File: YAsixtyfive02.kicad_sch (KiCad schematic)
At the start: 64 parts, among them J1 ~{NMI}, J2 Aux 5VDC, J3 Power 5V, J4 Expansion Bus, J7 GND, J8 FTDI Serial2USB, SW1 RESET, SW2 SW_Push_DPDT, U1 WD65C02, U10 74LS138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

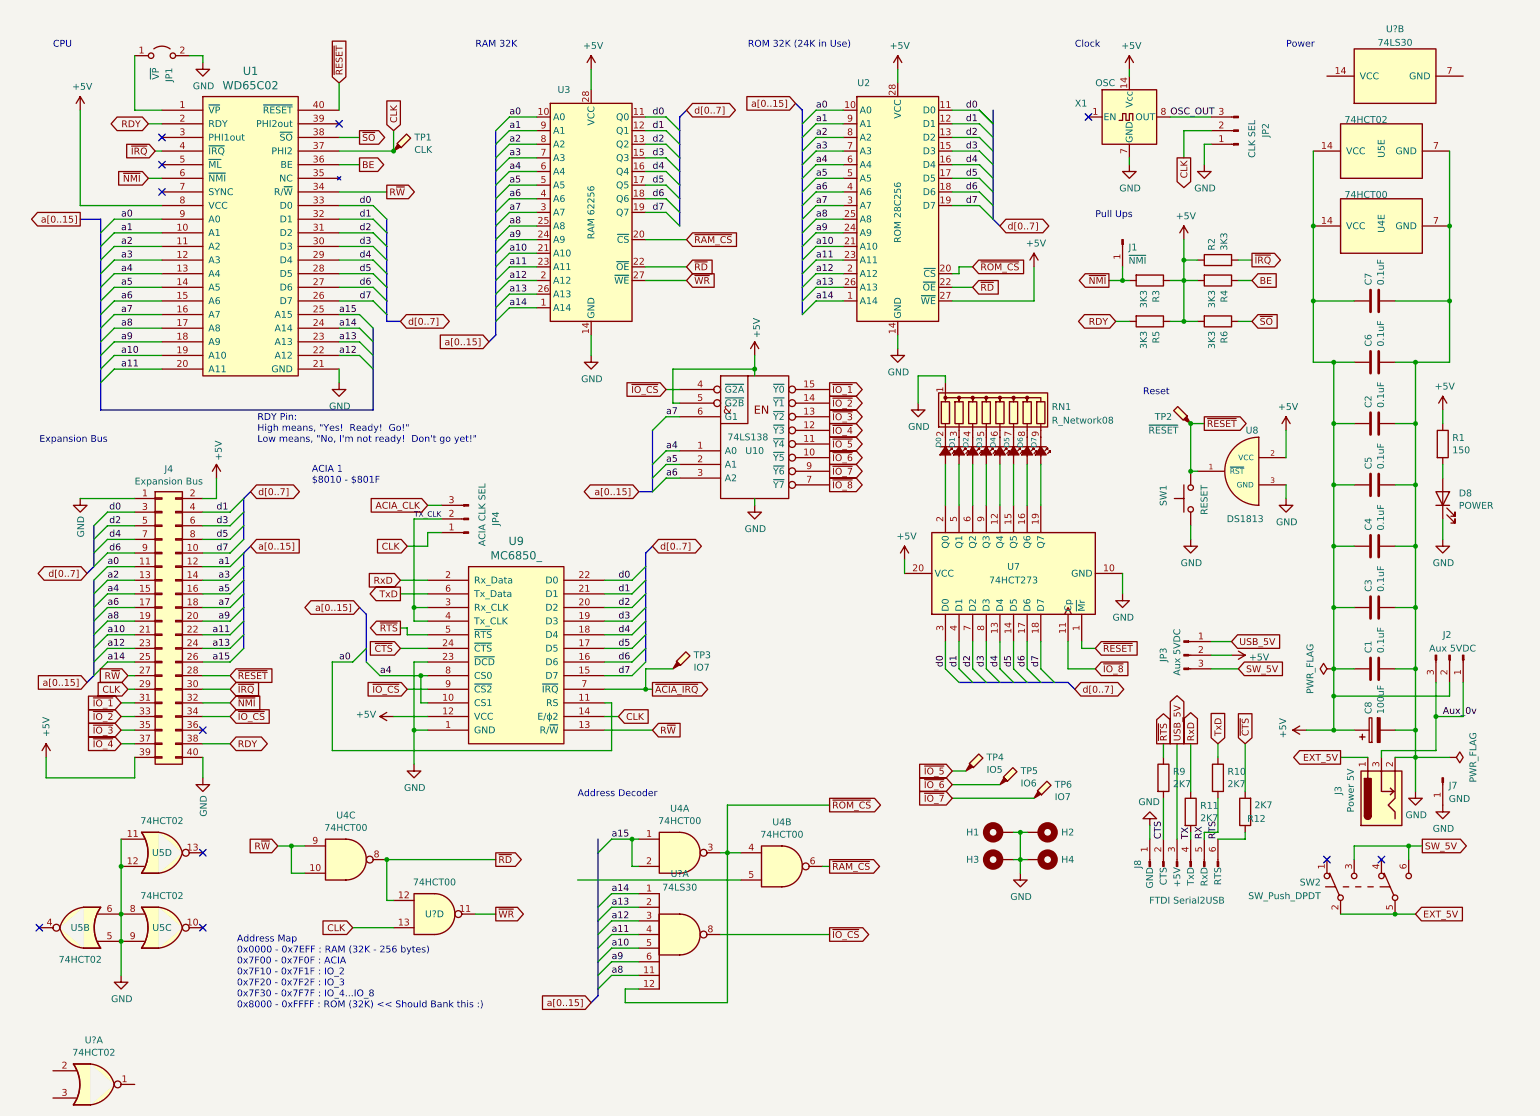
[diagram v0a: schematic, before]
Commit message: rev 1.6.0 ready new memory map
CPU/ROM/RAM/ACIA/SR New memory map, io in expansion port
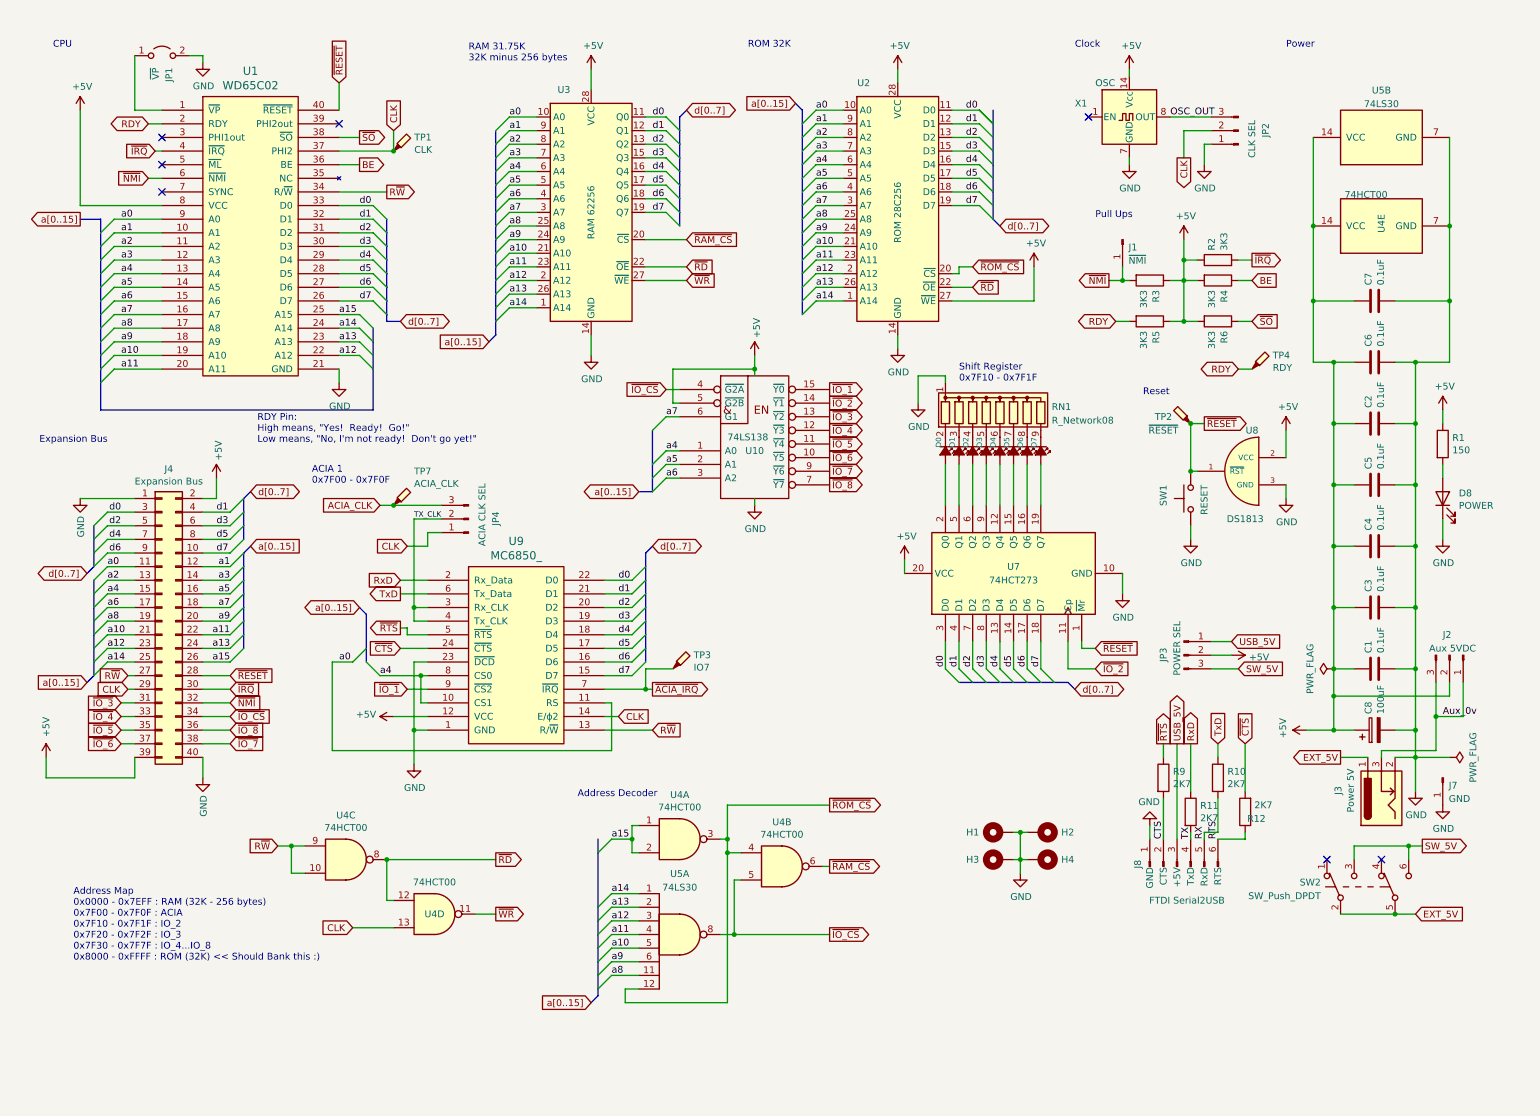
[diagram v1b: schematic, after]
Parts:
- removed TP5: IO6, TestPoint:TestPoint_THTPad_1.0x1.0mm_Drill0.5mm, symbol Connector:TestPoint_Probe
- removed TP6: IO7, TestPoint:TestPoint_THTPad_1.0x1.0mm_Drill0.5mm, symbol Connector:TestPoint_Probe
- removed U5, U?: 74HCT02, Package_DIP:DIP-14_W7.62mm_Socket_LongPads, symbol 74xx:74HCT02
- added TP7: ACIA_CLK, TestPoint:TestPoint_THTPad_2.0x2.0mm_Drill1.0mm, symbol Connector:TestPoint_Probe
- JP3: value Aux 5VDC -> POWER SEL
- TP4: value IO5 -> RDY
- U5: renamed from U?; footprint (none) -> Package_DIP:DIP-14_W7.62mm_Socket_LongPads
- gave numbers to parts that had none: 1
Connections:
- net +5V: now also U5.14 (VCC)
- net ACIA_CLK: now also TP7.1
- net GND: now also U5.7 (GND)
- net RDY: now also TP4.1; no longer J4.38 (Pin_38)
- net ~{IO_1}: now also U9.9 (~{CS2}); no longer J4.31 (Pin_31)
- net ~{IO_2}: now also U7.11 (Cp); no longer J4.33 (Pin_33)
- net ~{IO_3}: now also J4.31 (Pin_31); no longer J4.35 (Pin_35)
- net ~{IO_4}: now also J4.33 (Pin_33); no longer J4.37 (Pin_37)
- net ~{IO_5}: now also J4.35 (Pin_35); no longer TP4.1
- net ~{IO_6}: now also J4.37 (Pin_37)
- net ~{IO_7}: now also J4.38 (Pin_38)
- net ~{IO_8}: now also J4.36 (Pin_36); no longer U7.11 (Cp)
- net ~{IO_CS}: now also U4.5; no longer U9.9 (~{CS2})
- no-connect marks 11 -> 7
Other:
- note added: "ACIA 1 0x7F00 - 0x7F0F"
- note added: "RAM 31.75K 32K minus 256 bytes"
- note added: "ROM 32K"
- note added: "Shift Register 0x7F10 - 0x7F1F"
- note removed: "ACIA 1 $8010 - $801F"
- note removed: "RAM 32K"
- note removed: "ROM 32K (24K in Use)"
- moved on the sheet: TP4, U4A, U5B

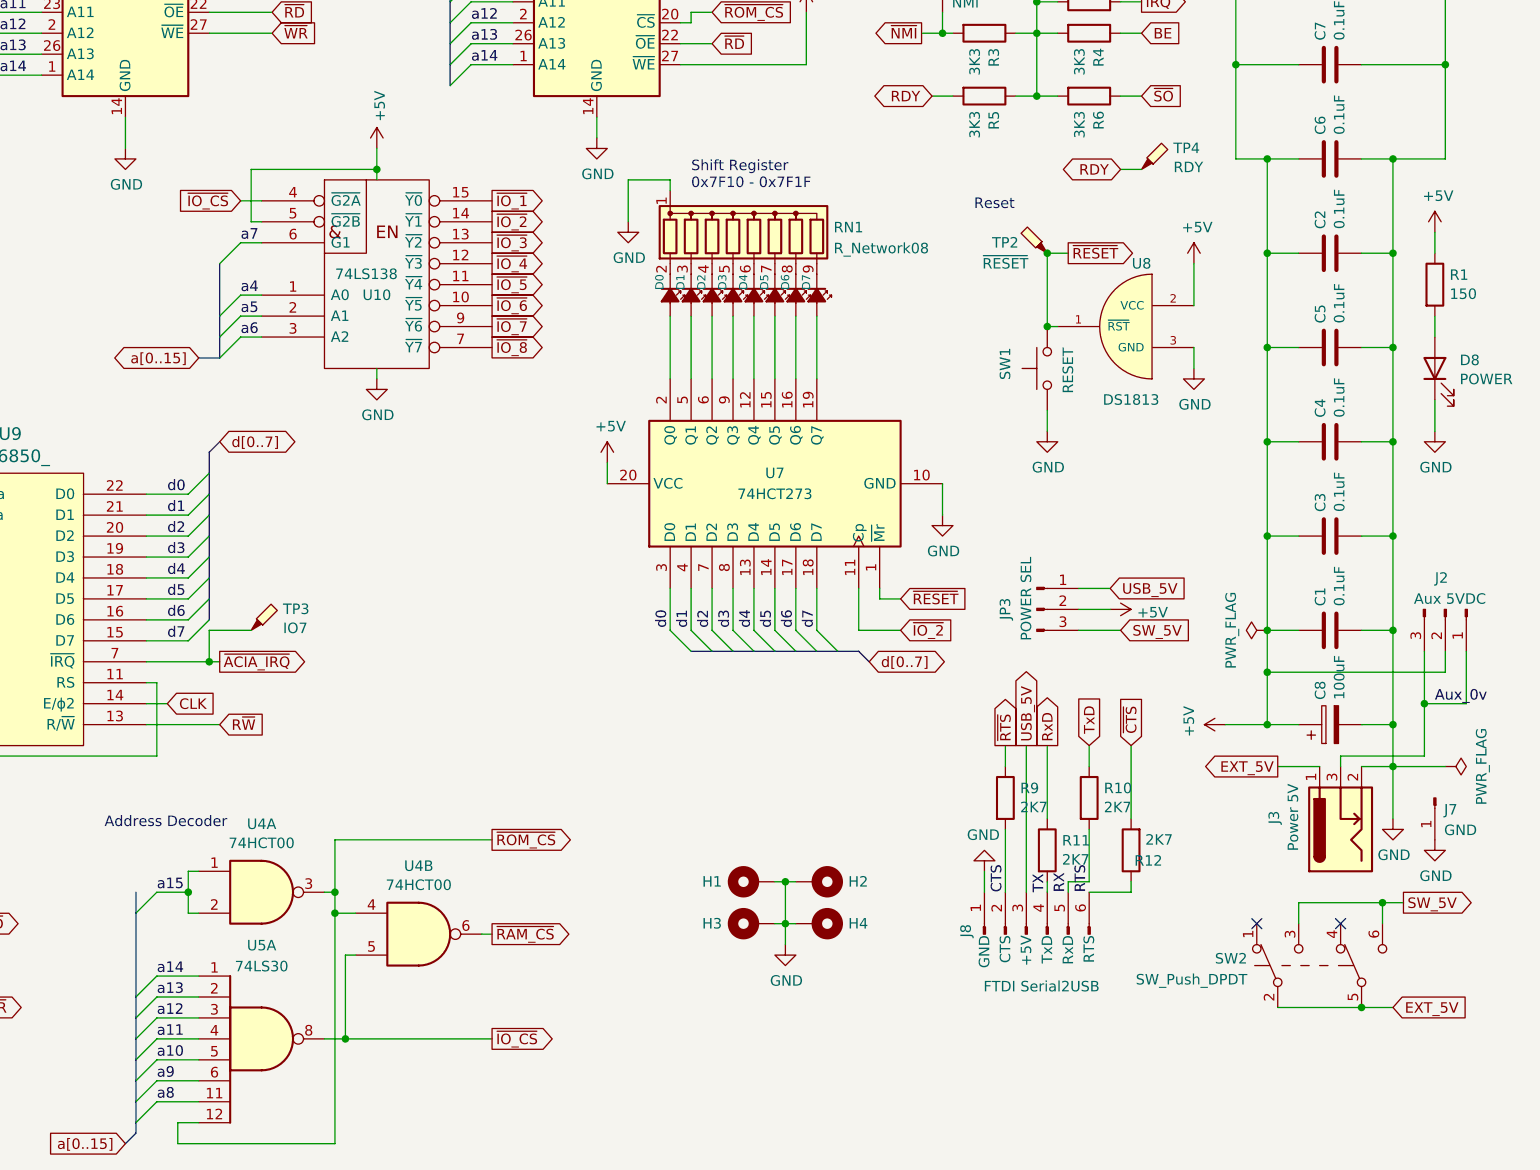
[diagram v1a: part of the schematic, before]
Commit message: rev 1.6.1 ready. minor routing updates and acia CS fixed
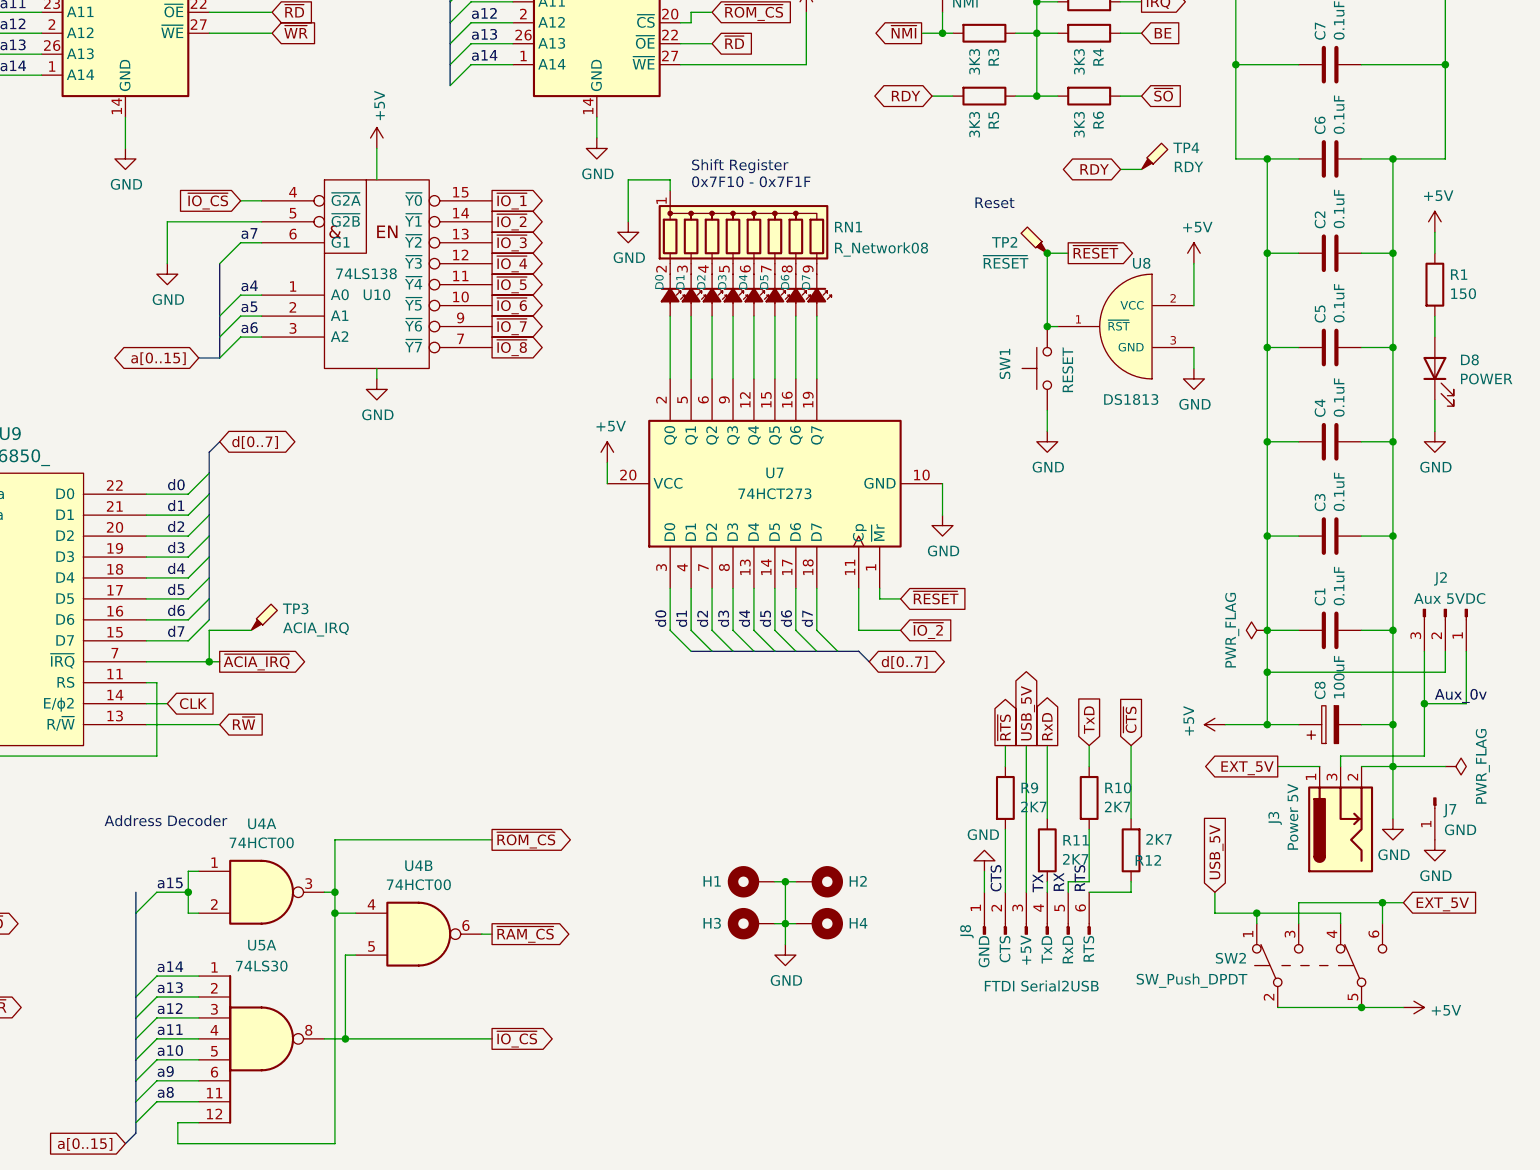
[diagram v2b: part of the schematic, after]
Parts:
- removed JP3: POWER SEL, Connector_PinHeader_2.54mm:PinHeader_1x03_P2.54mm_Vertical, symbol Connector:Conn_01x03_Male
- C8: footprint Capacitor_THT:CP_Radial_D8.0mm_P3.80mm -> Capacitor_THT:CP_Radial_D6.3mm_P2.50mm
- TP1, TP2, TP7: footprint TestPoint:TestPoint_THTPad_2.0x2.0mm_Drill1.0mm -> TestPoint:TestPoint_THTPad_1.5x1.5mm_Drill0.7mm
- TP3: value IO7 -> ACIA_IRQ
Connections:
- net SW_5V is gone; now on net EXT_5V: SW2.3 (C), SW2.6 (C)
- net +5V: now also SW2.2 (B), SW2.5 (B); no longer U10.5 (~{G2B})
- net EXT_5V: no longer SW2.2 (B), SW2.5 (B)
- net GND: now also U10.5 (~{G2B})
- net USB_5V: now also SW2.1 (A), SW2.4 (A)
- no-connect marks 7 -> 5
